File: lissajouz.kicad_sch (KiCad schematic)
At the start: 132 parts, among them J1 Barrel_Jack, J2 AudioJack3, Q1 BC557, Q10 2N7000, Q2 BC557, Q3 2N7000, Q4 BC557, Q5 BC557, Q6 2N7000, Q7 2N7000, Q8 2N7000, Q9 2N7000, SW1 ${SIM.PARAMS}, SW2 ${SIM.PARAMS}, U1 LM324, U2 LM324, U3 LM324

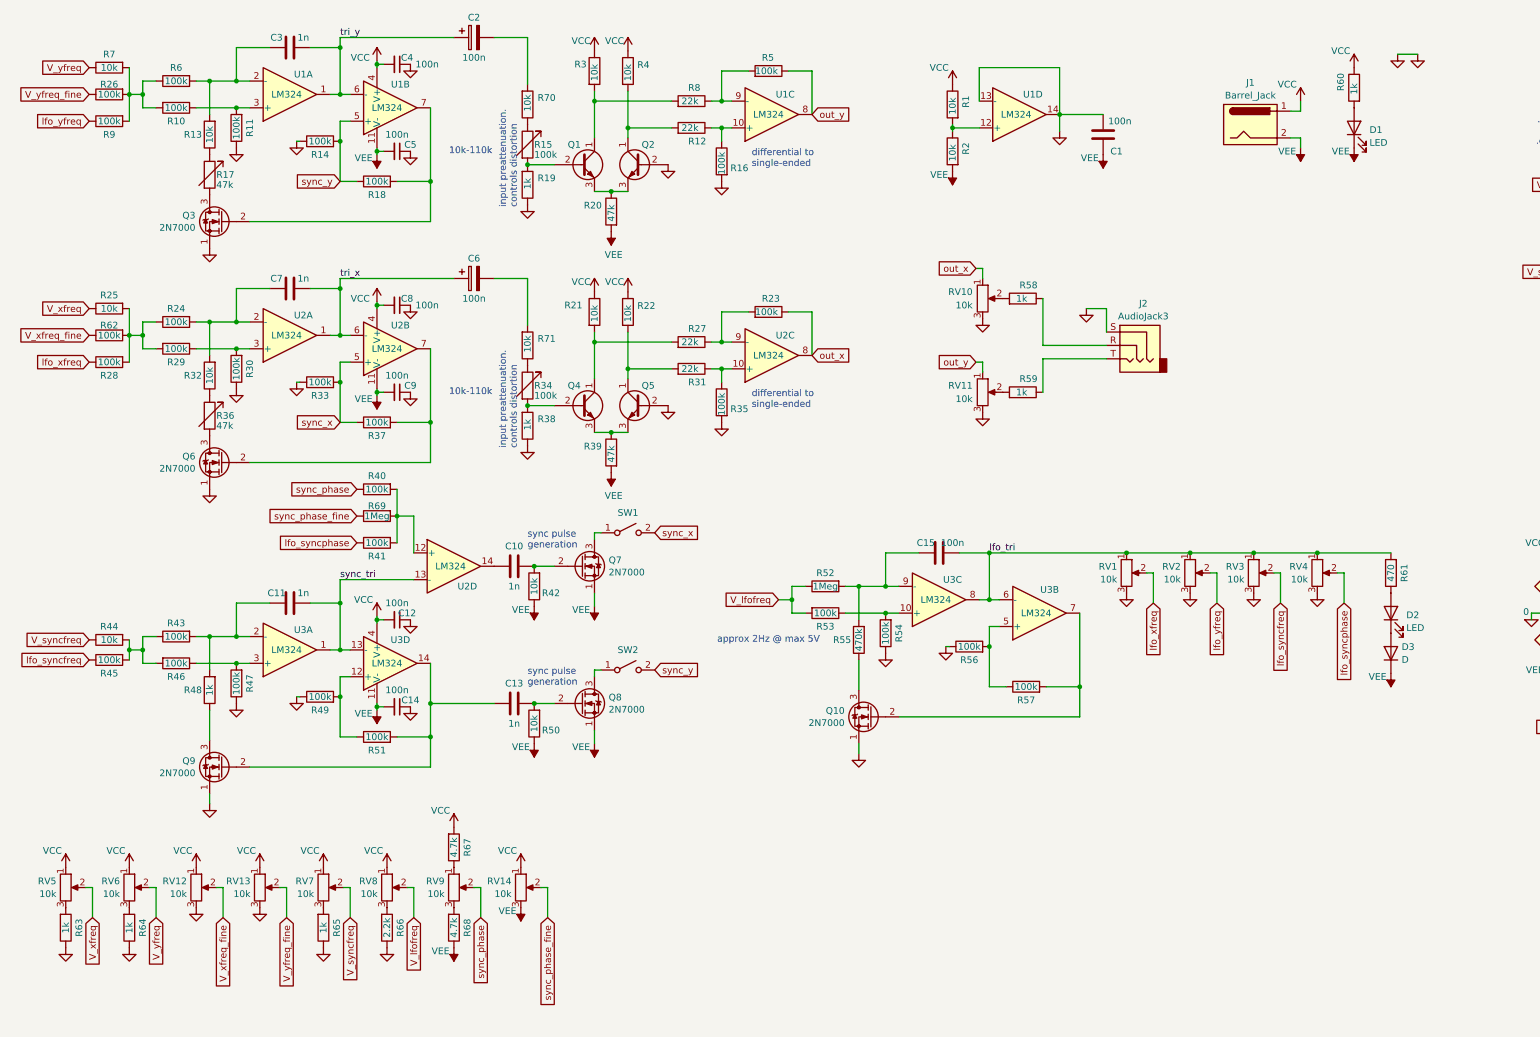
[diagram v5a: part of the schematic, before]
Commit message: Schematic fixes, did not update PCB yet!
- Darken LEDs by increasing resistors R60 and R61 to 10k each
- LFO LED: go closer to "dark" by adding second diode D4
- Move LFO frequency range down (decrease low-end R66 and add new top-end R72)
- Decrease minimum and maximum syncfreq range (4.7k R73 to GND)
- Increase "freq fine" resistors R26 and R62 to 470k
- Fix wrong BJT transistor values
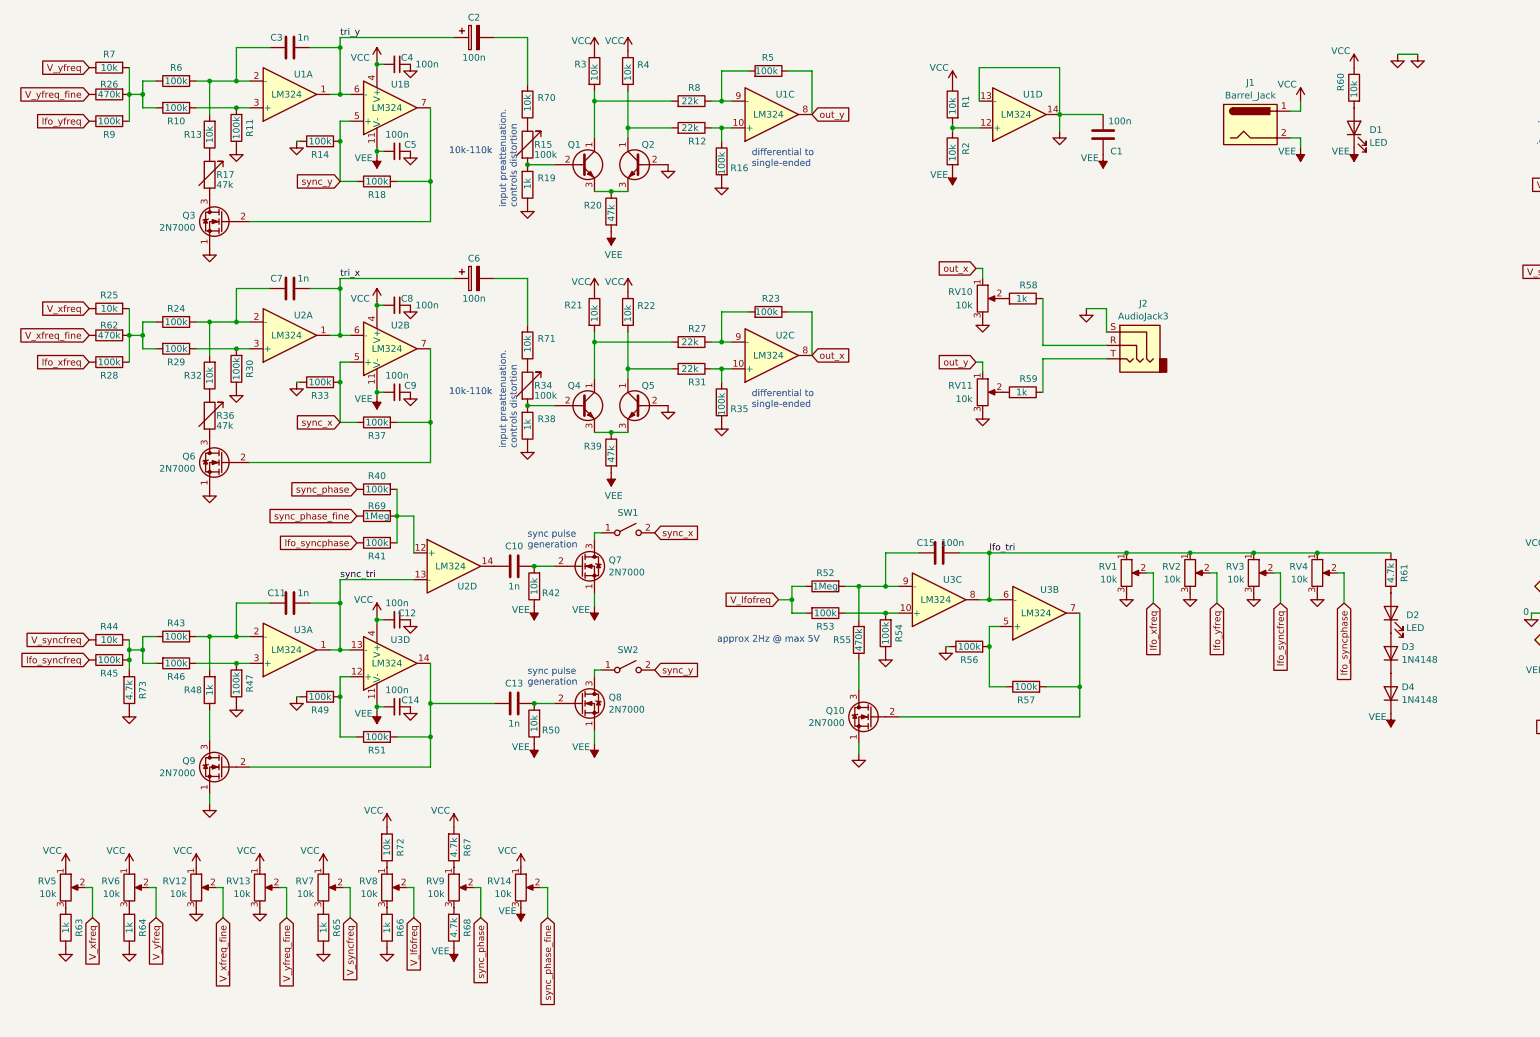
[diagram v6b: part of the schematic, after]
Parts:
- added D4: 1N4148, Diode_THT:D_5W_P12.70mm_Horizontal, symbol Device:D
- added R72: 10k, Resistor_SMD:R_0805_2012Metric_Pad1.20x1.40mm_HandSolder, symbol Device:R
- added R73: 4.7k, Resistor_SMD:R_0805_2012Metric_Pad1.20x1.40mm_HandSolder, symbol Device:R
- D3: value D -> 1N4148
- Q1, Q2, Q4, Q5: value BC557 -> BC547
- R26, R62: value 100k -> 470k
- R60: value 1k -> 10k
- R61: value 470 -> 4.7k
- R66: value 2.2k -> 1k
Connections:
- net GND: now also R73.1
- net VCC: now also R72.2; no longer RV8.1
- net VEE: now also D4.1 (K); no longer D3.1 (K)
- net at R43.1, R44.2, R45.2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: now also R73.2
- new net: D3.1 (K), D4.2 (A)
- new net: R72.1, RV8.1

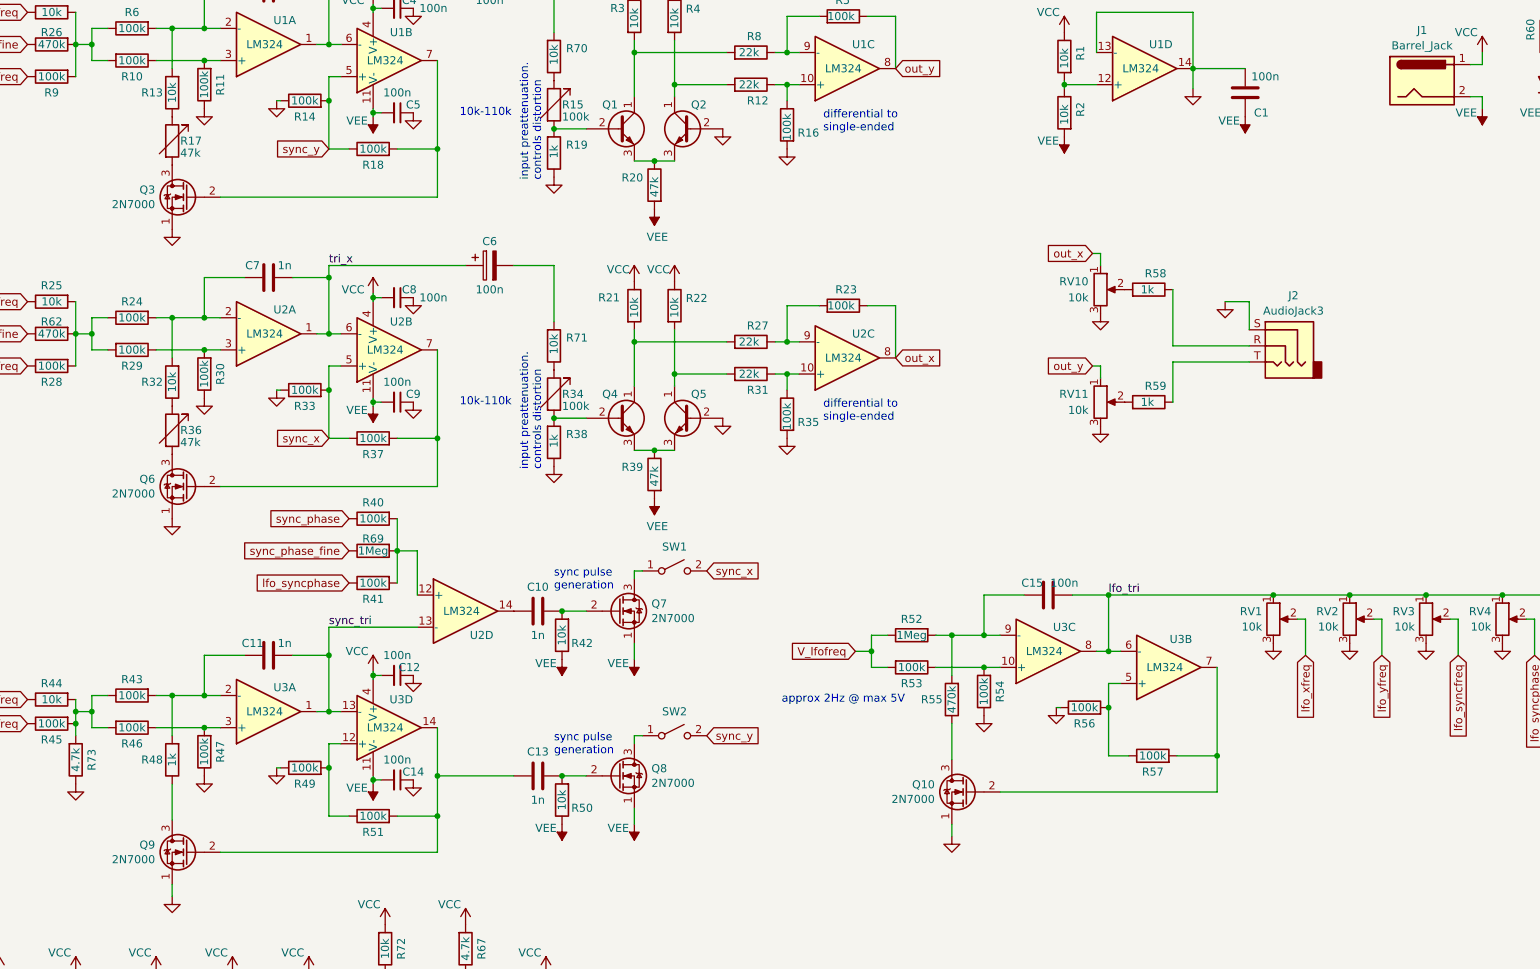
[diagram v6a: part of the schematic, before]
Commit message: Fine-tuning and fix switch footprint
- fine-tune slant poti range
- reduce x/y freq lfo when not synced
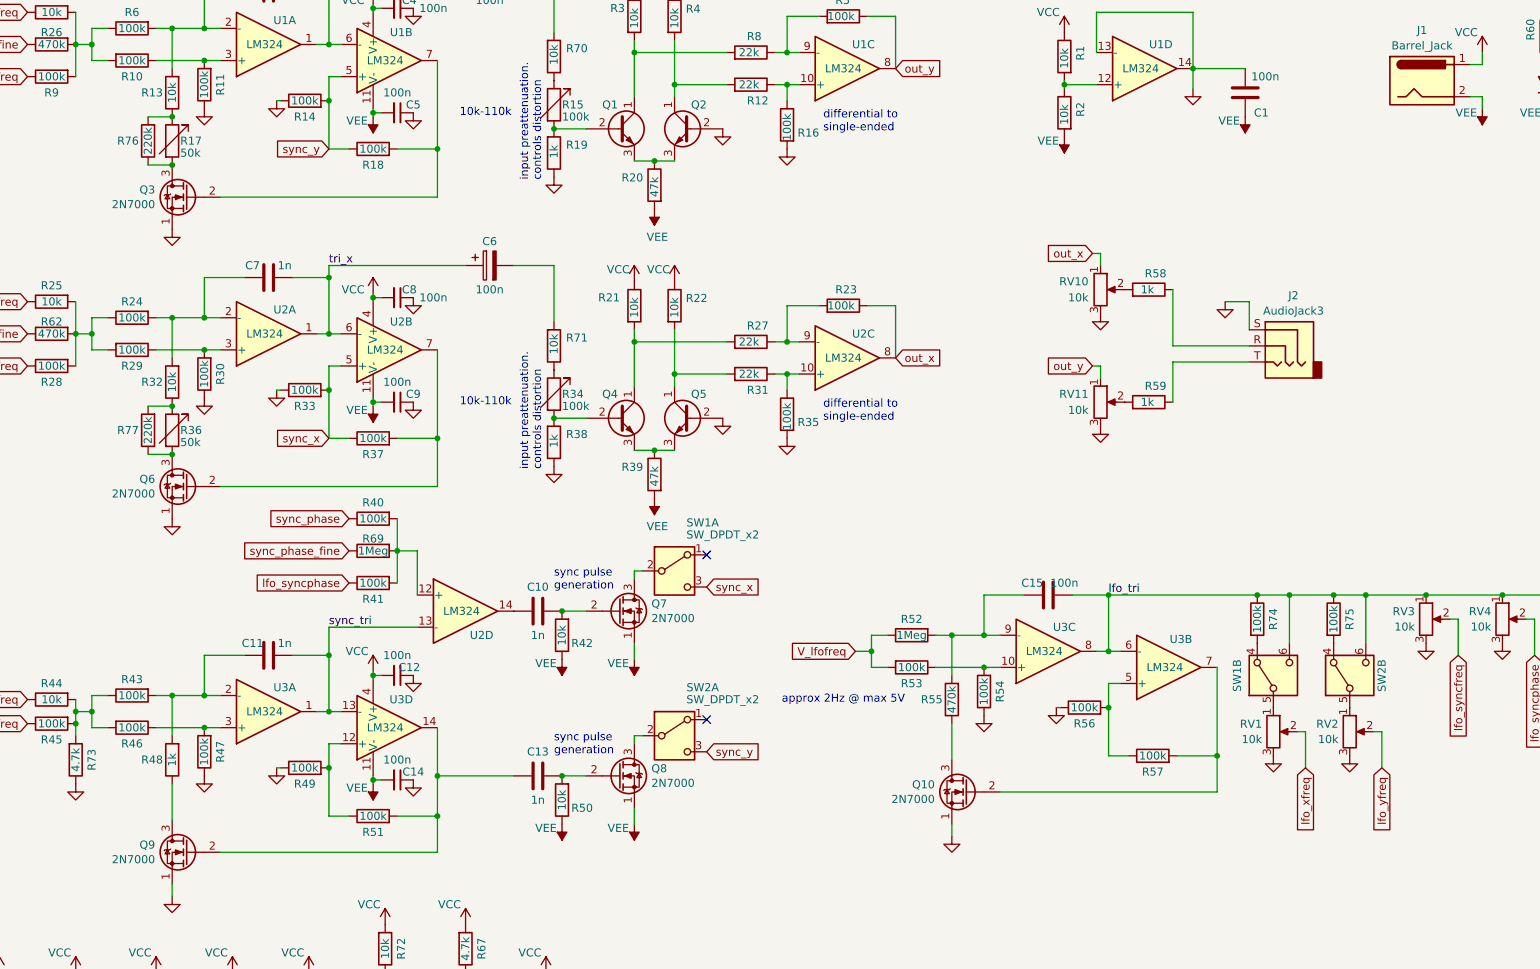
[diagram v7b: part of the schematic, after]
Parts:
- removed SW1, SW2: ${SIM.PARAMS}, footprints:switch8x8, symbol Switch:SW_SPST
- added R74, R75: 100k, Resistor_SMD:R_0805_2012Metric_Pad1.20x1.40mm_HandSolder, symbol Device:R
- added R76, R77: 220k, Resistor_SMD:R_0805_2012Metric_Pad1.20x1.40mm_HandSolder, symbol Device:R
- added SW1, SW2: SW_DPDT_x2, symbol Switch:SW_DPDT_x2
- R17, R36: value 47k -> 50k
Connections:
- net lfo_tri: now also R74.1, R75.1, SW1.6 (C), SW2.6 (C); no longer RV1.1, RV2.1
- net sync_x: now also SW1.3 (C)
- net sync_y: now also SW2.3 (C)
- net at Q7.3 (D): now also SW1.2 (B)
- net at Q8.3 (D): now also SW2.2 (B)
- net at R13.1, R17.1: now also R76.2
- net at R32.1, R36.1: now also R77.2
- net at Q6.3 (D), R36.2: now also R77.1
- net at Q3.3 (D), R17.2: now also R76.1
- new net: RV2.1, SW2.5 (B)
- new net: R75.2, SW2.4 (A)
- new net: R74.2, SW1.4 (A)
- new net: RV1.1, SW1.5 (B)
- no-connect marks 0 -> 2
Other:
- moved on the sheet: RV1, RV2

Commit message: Fix bugs in PCB
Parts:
- D3, D4: footprint Diode_THT:D_5W_P12.70mm_Horizontal -> Diode_THT:D_DO-35_SOD27_P7.62mm_Horizontal
- SW1, SW2: footprint (none) -> footprints:switch8x8
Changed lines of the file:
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@@
 			)
 		)
-		(property "Footprint" "Diode_THT:D_5W_P12.70mm_Horizontal"
+		(property "Footprint" "Diode_THT:D_DO-35_SOD27_P7.62mm_Horizontal"
 			(at 274.32 139.7 0)
 			(effects
@@
 			)
 		)
-		(property "Footprint" ""
+		(property "Footprint" "footprints:switch8x8"
 			(at 236.22 125.73 0)
 			(effects
@@
 			)
 		)
-		(property "Footprint" "Diode_THT:D_5W_P12.70mm_Horizontal"
+		(property "Footprint" "Diode_THT:D_DO-35_SOD27_P7.62mm_Horizontal"
 			(at 274.32 132.08 0)
 			(effects
@@
 			)
 		)
-		(property "Footprint" ""
+		(property "Footprint" "footprints:switch8x8"
 			(at 129.54 135.255 0)
 			(effects
@@
 			)
 		)
-		(property "Footprint" ""
+		(property "Footprint" "footprints:switch8x8"
 			(at 224.155 125.73 0)
 			(effects
@@
 			)
 		)
-		(property "Footprint" ""
+		(property "Footprint" "footprints:switch8x8"
 			(at 129.54 109.22 0)
 			(effects
